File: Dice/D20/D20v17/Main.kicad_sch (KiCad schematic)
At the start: 30 parts, among them J1 Conn_01x14, J2 Conn_01x04, J4 DNP, U1 NRF52810-CAAA-R, U2 KXTJ3-1057, U4 M24C02-FMH6TG, U8 SL1605, Y1 32MHz 40ppm

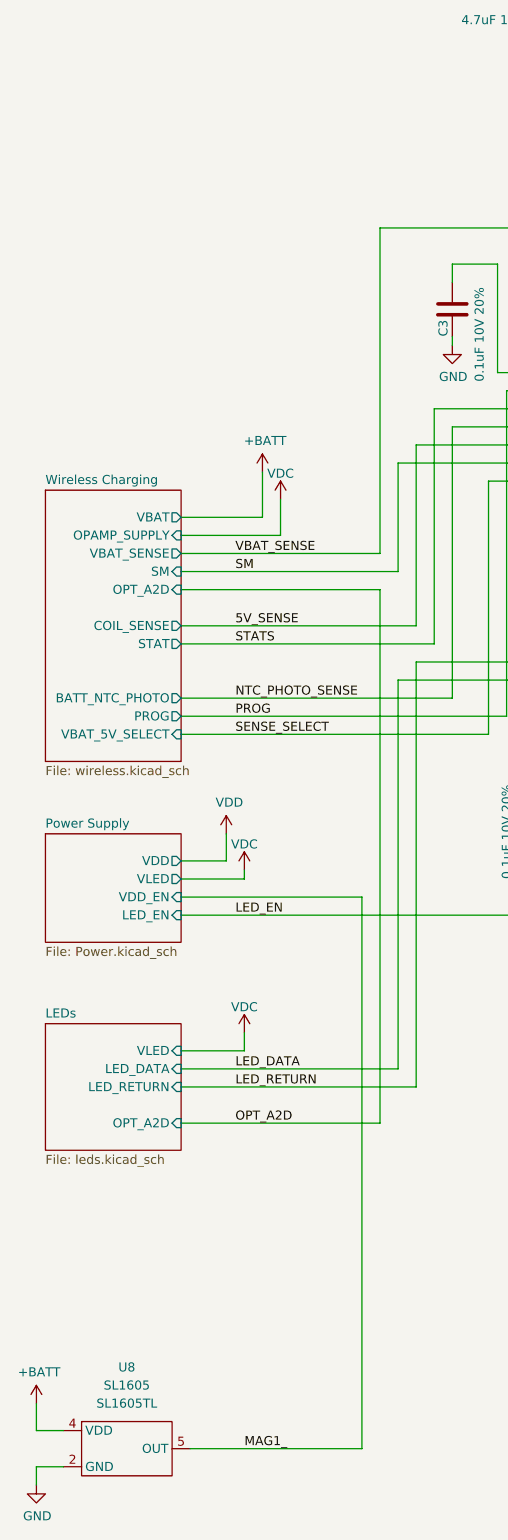
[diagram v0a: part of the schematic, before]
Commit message: Updated schematic Titles in D20V17 and likes, added 12mm D6 and Charging Jig
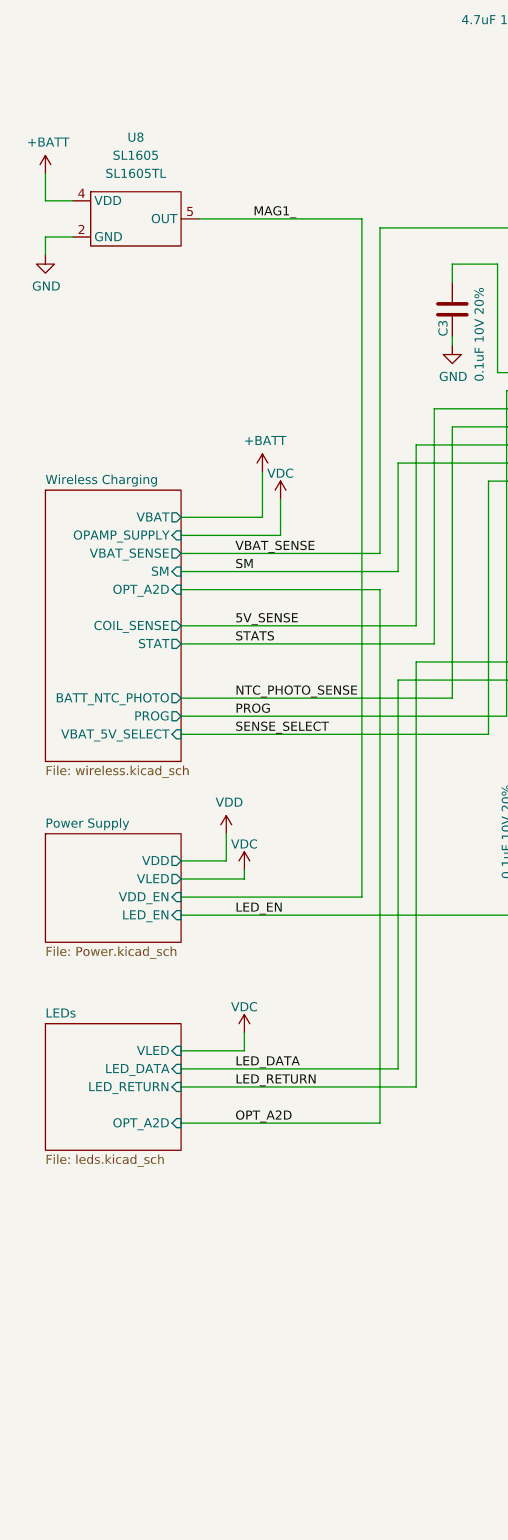
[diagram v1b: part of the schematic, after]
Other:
- title: Pixels D20 Schematic, Main -> Pixels D20V17 Schematic, Main
- moved on the sheet: U8
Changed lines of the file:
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@@
 	(paper "A4")
 	(title_block
-		(title "Pixels D20 Schematic, Main")
-		(date "2022-08-26")
+		(title "Pixels D20V17 Schematic, Main")
+		(date "2025-10-10")
 		(rev "13")
 		(company "Systemic Games, LLC")
@@
 	(wire
 		(pts
-			(xy 40.64 227.33) (xy 64.77 227.33)
+			(xy 41.91 54.61) (xy 64.77 54.61)
 		)
 		(stroke
@@
 	(wire
 		(pts
-			(xy 19.05 220.98) (xy 19.05 224.79)
+			(xy 20.32 48.26) (xy 20.32 52.07)
 		)
 		(stroke
@@
 	(wire
 		(pts
-			(xy 64.77 149.86) (xy 64.77 227.33)
+			(xy 64.77 149.86) (xy 64.77 54.61)
 		)
 		(stroke
@@
 	(wire
 		(pts
-			(xy 22.86 229.87) (xy 19.05 229.87)
+			(xy 24.13 57.15) (xy 20.32 57.15)
 		)
 		(stroke
@@
 	(wire
 		(pts
-			(xy 19.05 229.87) (xy 19.05 232.41)
+			(xy 20.32 57.15) (xy 20.32 59.69)
 		)
 		(stroke
@@
 	(wire
 		(pts
-			(xy 19.05 224.79) (xy 22.86 224.79)
+			(xy 20.32 52.07) (xy 24.13 52.07)
 		)
 		(stroke
@@
 	)
 	(label "MAG1_"
-		(at 48.26 227.33 0)
+		(at 49.53 54.61 0)
 		(effects
 			(font
@@
 	(symbol
 		(lib_id "power:GND")
-		(at 19.05 232.41 0)
+		(at 20.32 59.69 0)
 		(unit 1)
 		(exclude_from_sim no)
@@
 		(dnp no)
 		(property "Reference" "#PWR045"
-			(at 19.05 238.76 0)
+			(at 20.32 66.04 0)
 			(effects
 				(font
@@
 		)
 		(property "Value" "GND"
-			(at 19.177 236.8042 0)
+			(at 20.447 64.0842 0)
 			(effects
 				(font
@@
 		)
 		(property "Footprint" ""
-			(at 19.05 232.41 0)
+			(at 20.32 59.69 0)
 			(effects
 				(font
@@
 		)
 		(property "Datasheet" ""
-			(at 19.05 232.41 0)
+			(at 20.32 59.69 0)
 			(effects
 				(font
@@
 		)
 		(property "Description" ""
-			(at 19.05 232.41 0)
+			(at 20.32 59.69 0)
 			(effects
 				(font
@@
 	(symbol
 		(lib_id "power:+BATT")
-		(at 19.05 220.98 0)
+		(at 20.32 48.26 0)
 		(unit 1)
 		(exclude_from_sim no)
@@
 		(dnp no)
 		(property "Reference" "#PWR017"
-			(at 19.05 224.79 0)
+			(at 20.32 52.07 0)
 			(effects
 				(font
@@
 		)
 		(property "Value" "+BATT"
-			(at 19.431 216.5858 0)
+			(at 20.701 43.8658 0)
 			(effects
 				(font
@@
 		)
 		(property "Footprint" ""
-			(at 19.05 220.98 0)
+			(at 20.32 48.26 0)
 			(effects
 				(font
@@
 		)
 		(property "Datasheet" ""
-			(at 19.05 220.98 0)
+			(at 20.32 48.26 0)
 			(effects
 				(font
@@
 		)
 		(property "Description" ""
-			(at 19.05 220.98 0)
+			(at 20.32 48.26 0)
 			(effects
 				(font
@@
 	(symbol
 		(lib_id "Pixels-dice:SL1605")
-		(at 31.75 227.33 0)
+		(at 33.02 54.61 0)
 		(unit 1)
 		(exclude_from_sim no)
@@
 		(fields_autoplaced yes)
 		(property "Reference" "U8"
-			(at 31.75 215.9 0)
+			(at 33.02 43.18 0)
 			(effects
 				(font
@@
 		)
 		(property "Value" "SL1605"
-			(at 31.75 218.44 0)
+			(at 33.02 45.72 0)
 			(effects
 				(font
@@
 		)
 		(property "Footprint" "Package_TO_SOT_SMD:SOT-553"
-			(at 31.75 227.33 0)
+			(at 33.02 54.61 0)
 			(effects
 				(font
@@
 		)
 		(property "Datasheet" ""
-			(at 31.75 227.33 0)
+			(at 33.02 54.61 0)
 			(effects
 				(font
@@
 		)
 		(property "Description" ""
-			(at 31.75 227.33 0)
+			(at 33.02 54.61 0)
 			(effects
 				(font
@@
 		)
 		(property "Manufacturer" "Slkor(SLKORMICRO Elec.)"
-			(at 31.75 227.33 0)
+			(at 33.02 54.61 0)
 			(effects
 				(font
@@
 		)
 		(property "Part Number" "SL1605TL"
-			(at 31.75 220.98 0)
+			(at 33.02 48.26 0)
 			(effects
 				(font
@@
 		)
 		(property "LCSC Part #" "C2826474"
-			(at 31.75 227.33 0)
+			(at 33.02 54.61 0)
 			(effects
 				(font
